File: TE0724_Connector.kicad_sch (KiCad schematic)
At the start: 1 part, among them J1 SS5-80-3.50-X-D-K-XX

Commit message: fixed 3D models
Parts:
- J1: value SS5-80-3.50-X-D-K-XX -> SS5-80-3.50-L-D-K-TR
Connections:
- no-connect marks 116 -> 113

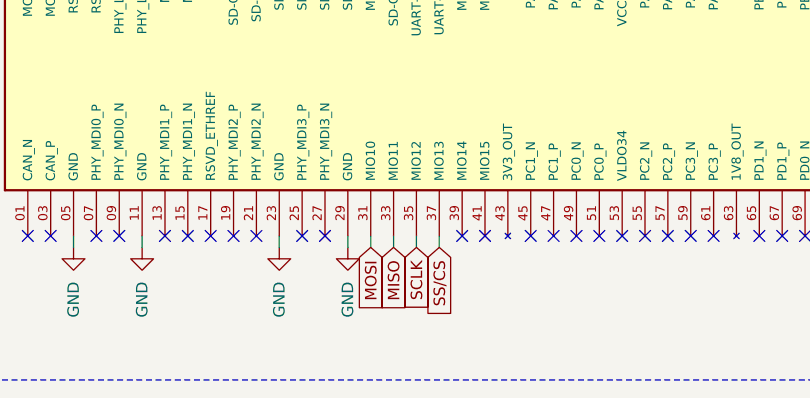
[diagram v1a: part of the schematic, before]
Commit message: Removed SPI Connections
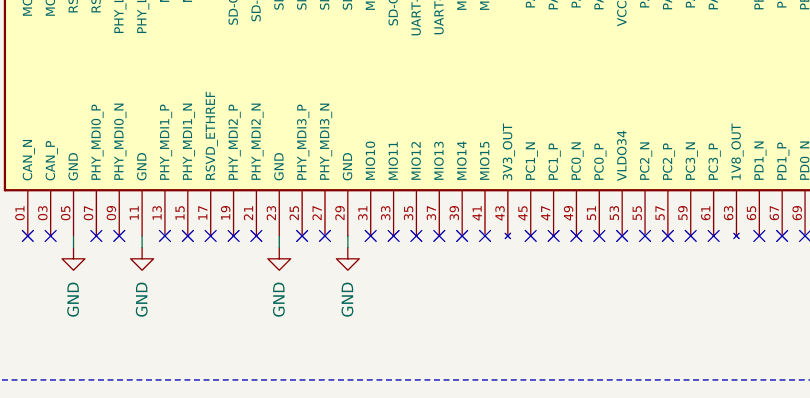
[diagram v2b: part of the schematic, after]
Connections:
- net MISO: no longer names the net of J1.33 (MIO11)
- net MOSI: no longer names the net of J1.31 (MIO10)
- net SCLK: no longer names the net of J1.35 (MIO12)
- net SS/CS: no longer names the net of J1.37 (MIO13)
- no-connect marks 113 -> 117
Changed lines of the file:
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@@
+	)
+	(no_connect
+		(at 92.71 102.87)
 	)
 	(no_connect
@@
 	)
 	(no_connect
+		(at 95.25 102.87)
+	)
+	(no_connect
 		(at 161.29 102.87)
 	)
@@
 	)
 	(no_connect
+		(at 87.63 102.87)
+	)
+	(no_connect
 		(at 184.15 102.87)
 	)
@@
 	)
 	(no_connect
+		(at 90.17 102.87)
+	)
+	(no_connect
 		(at 219.71 102.87)
 	)
@@
 	(wire
 		(pts
-			(xy 87.63 104.14) (xy 87.63 102.87)
-		)
-		(stroke
-			(width 0)
-			(type default)
-		)
-	)
-	(wire
-		(pts
 			(xy 55.88 58.42) (xy 55.88 59.69)
 		)
@@
 	(wire
 		(pts
-			(xy 95.25 104.14) (xy 95.25 102.87)
-		)
-		(stroke
-			(width 0)
-			(type default)
-		)
-	)
-	(wire
-		(pts
 			(xy 201.93 58.42) (xy 201.93 67.31)
 		)
@@
 	(wire
 		(pts
-			(xy 90.17 104.14) (xy 90.17 102.87)
-		)
-		(stroke
-			(width 0)
-			(type default)
-		)
-	)
-	(wire
-		(pts
 			(xy 95.25 67.31) (xy 95.25 66.04)
 		)
@@
 		(pts
 			(xy 77.47 104.14) (xy 77.47 102.87)
-		)
-		(stroke
-			(width 0)
-			(type default)
-		)
-	)
-	(wire
-		(pts
-			(xy 92.71 104.14) (xy 92.71 102.87)
 		)
 		(stroke
@@
 		)
 	)
-	(global_label "SS{slash}CS"
-		(shape input)
-		(at 95.25 104.14 270)
-		(fields_autoplaced yes)
-		(effects
-			(font
-				(size 1.27 1.27)
-			)
-			(justify right)
-		)
-		(property "Intersheetrefs" "${INTERSHEET_REFS}"
-			(at 95.25 113.3542 90)
-			(effects
-				(font
-					(size 1.27 1.27)
-				)
-				(justify right)
-				(hide yes)
-			)
-		)
-	)
 	(global_label "UART_RX"
 		(shape input)
@@
 				(hide yes)
 			)
-		)
-	)
-	(global_label "MOSI"
-		(shape input)
-		(at 87.63 104.14 270)
-		(fields_autoplaced yes)
-		(effects
-			(font
-				(size 1.27 1.27)
-			)
-			(justify right)
-		)
-		(property "Intersheetrefs" "${INTERSHEET_REFS}"
-			(at 87.63 111.7214 90)
-			(effects
-				(font
-					(size 1.27 1.27)
-				)
-				(justify right)
-				(hide yes)
-			)
-		)
-	)
-	(global_label "MISO"
-		(shape input)
-		(at 90.17 104.14 270)
-		(fields_autoplaced yes)
-		(effects
-			(font
-				(size 1.27 1.27)
-			)
-			(justify right)
-		)
-		(property "Intersheetrefs" "${INTERSHEET_REFS}"
-			(at 90.17 111.7214 90)
-			(effects
-				(font
-					(size 1.27 1.27)
-				)
-				(justify right)
-				(hide yes)
-			)
-		)
-	)
-	(global_label "SCLK"
-		(shape input)
-		(at 92.71 104.14 270)
-		(fields_autoplaced yes)
-		(effects
-			(font
-				(size 1.27 1.27)
-			)
-			(justify right)
-		)
-		(property "Intersheetrefs" "${INTERSHEET_REFS}"
-			(at 92.71 111.9028 90)
-			(effects
-				(font
-					(size 1.27 1.27)
-				)
-				(justify right)
-				(hide yes)
-			)

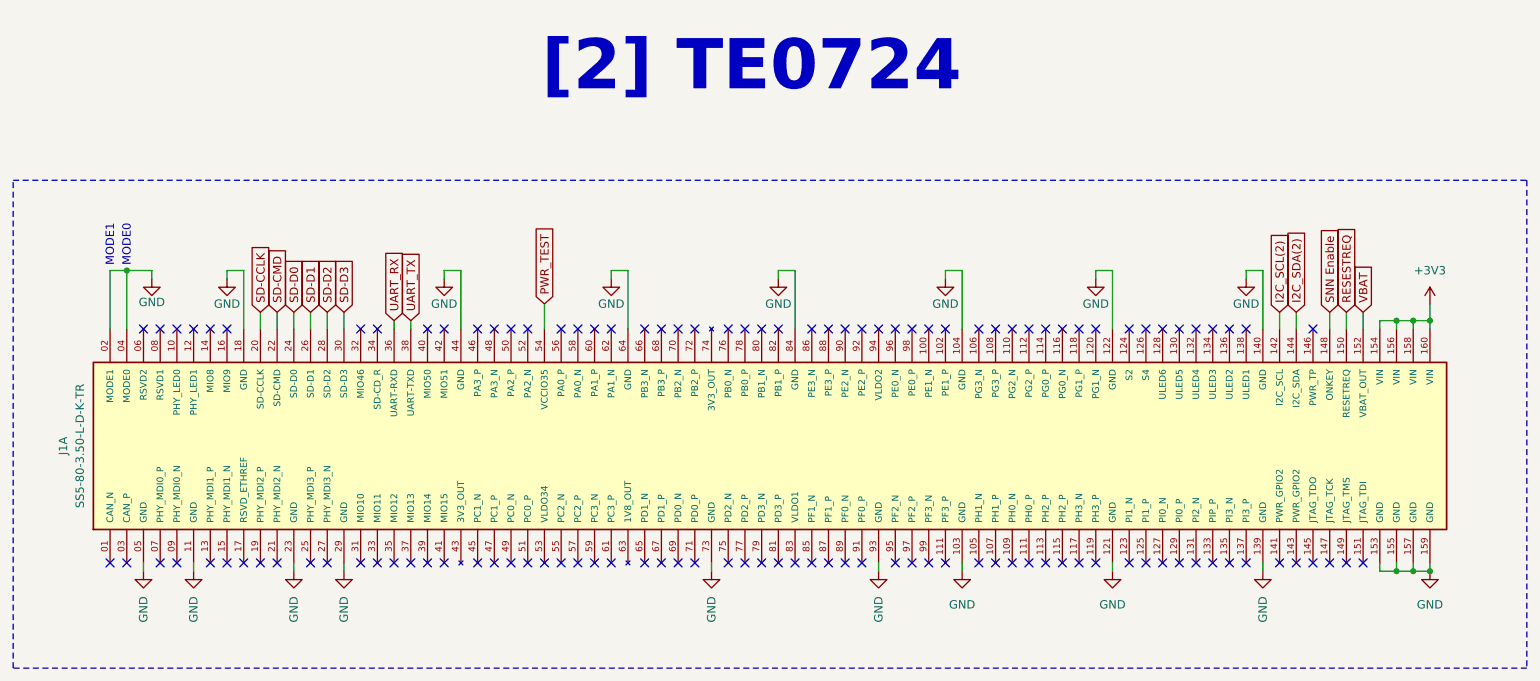
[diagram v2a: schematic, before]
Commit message: Added hierarchical lables to the schematic
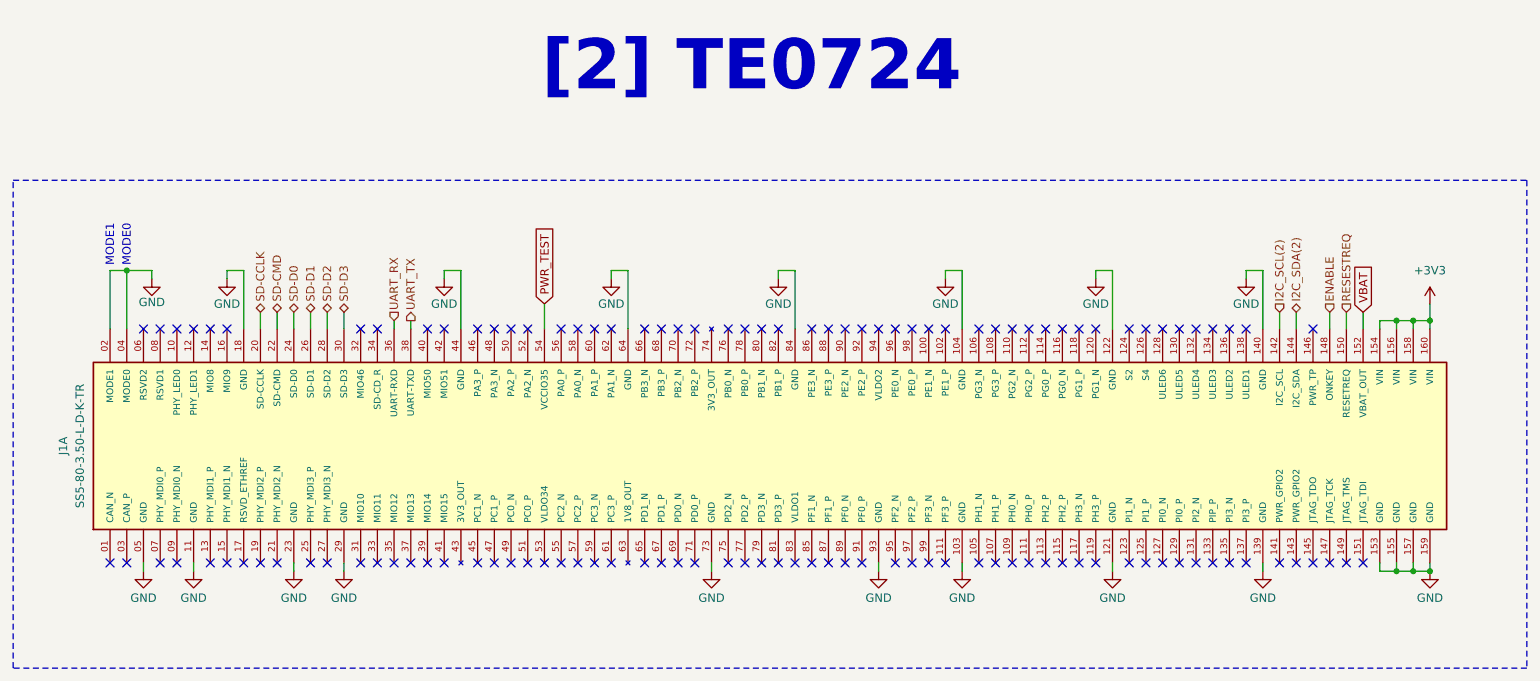
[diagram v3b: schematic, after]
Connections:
- net SNN Enable renamed ENABLE
